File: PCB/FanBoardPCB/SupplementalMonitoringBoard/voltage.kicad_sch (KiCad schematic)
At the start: 6 parts, among them U1 OPA842xDBV

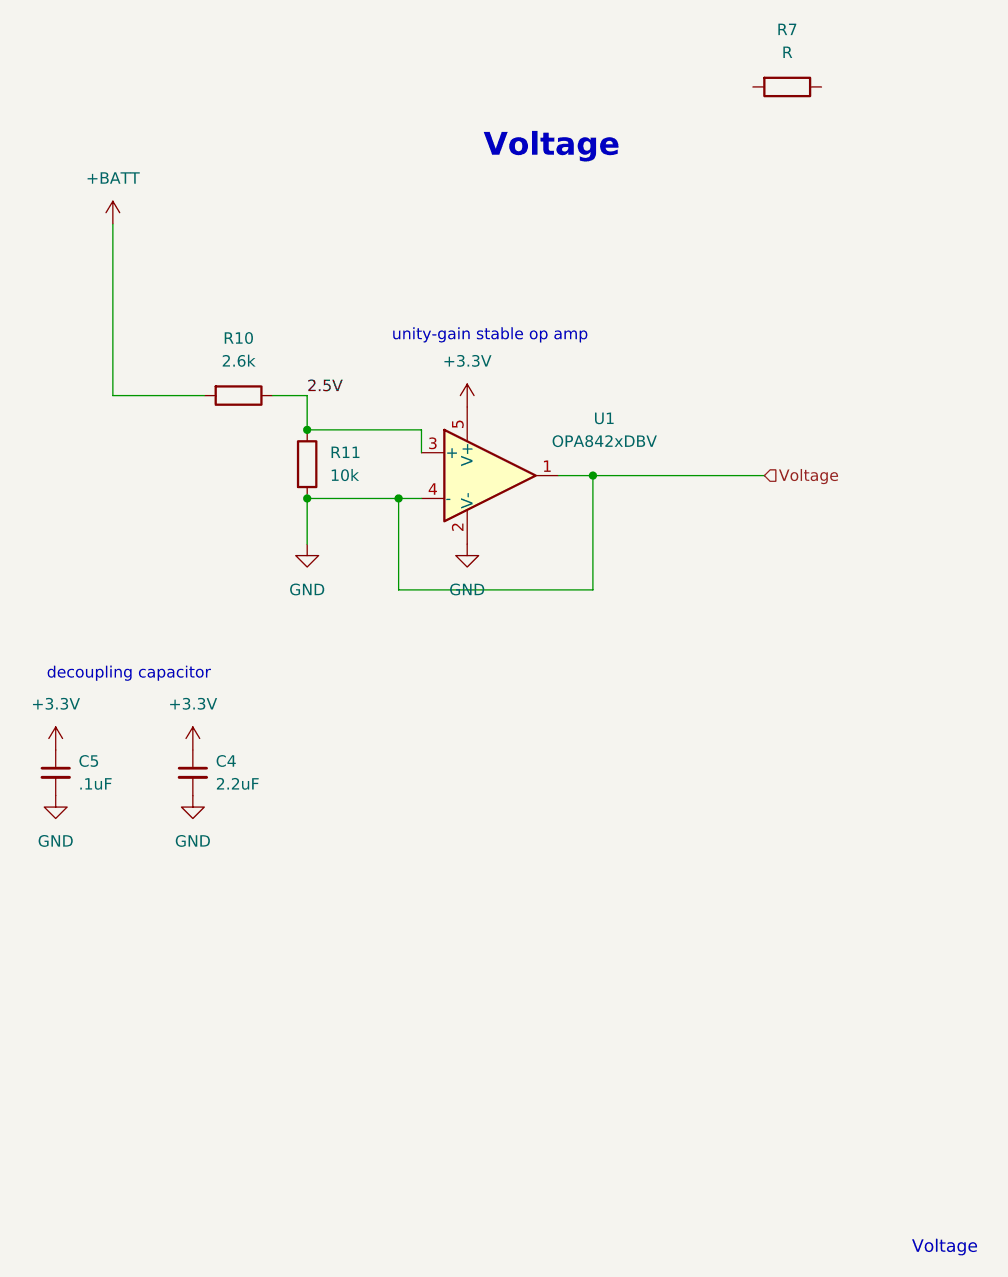
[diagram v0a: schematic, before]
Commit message: Supplemental Monitoring Board
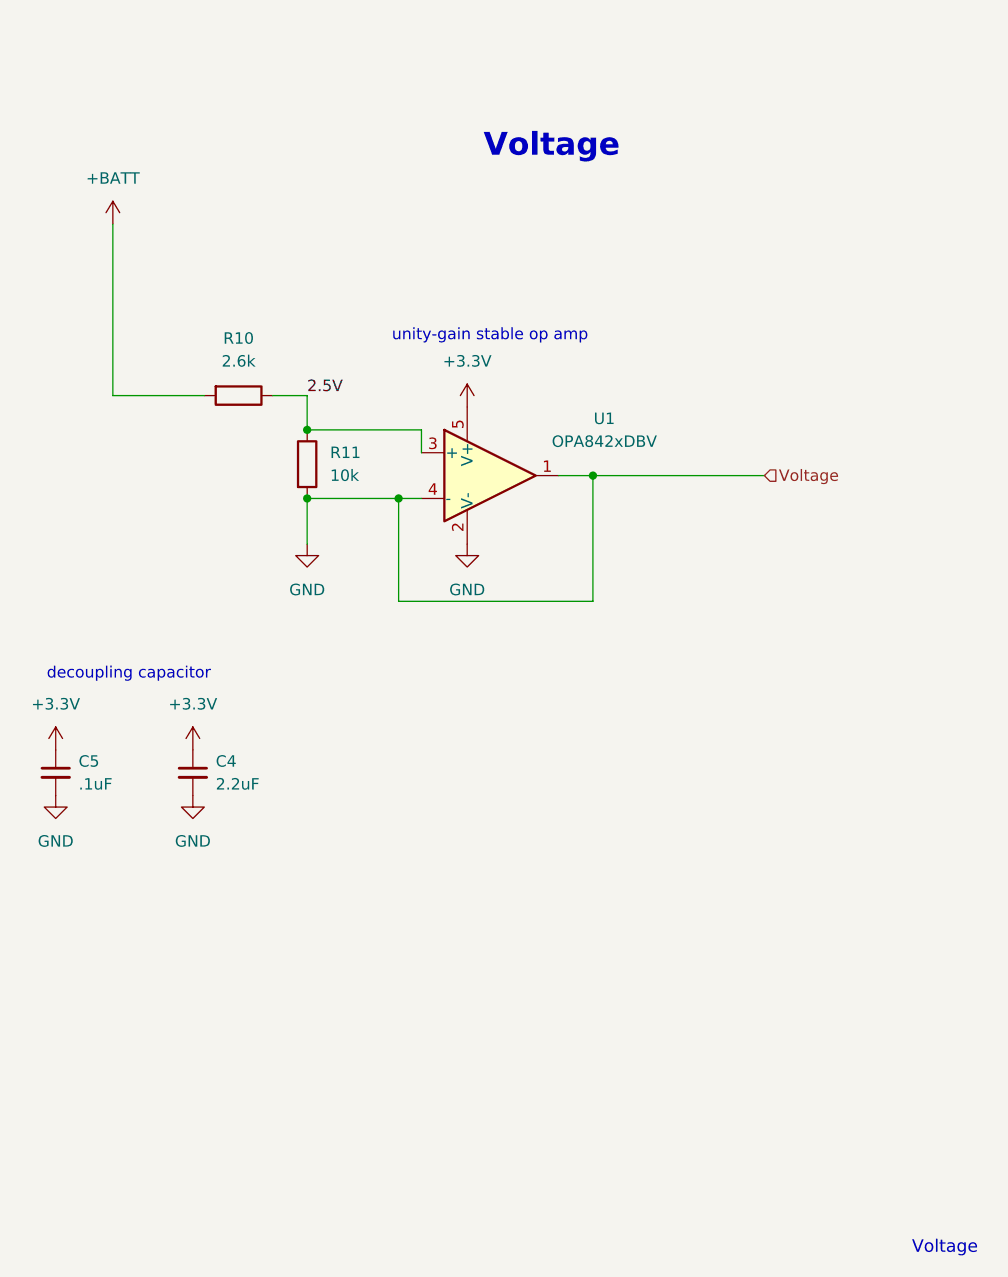
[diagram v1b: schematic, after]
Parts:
- removed R7: R, symbol Device:R
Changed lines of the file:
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@@
 	(wire
 		(pts
-			(xy 129.54 116.84) (xy 151.13 116.84)
-		)
-		(stroke
-			(width 0)
-			(type default)
-		)
-	)
-	(wire
-		(pts
-			(xy 129.54 106.68) (xy 129.54 116.84)
+			(xy 129.54 118.11) (xy 151.13 118.11)
+		)
+		(stroke
+			(width 0)
+			(type default)
+		)
+	)
+	(wire
+		(pts
+			(xy 129.54 106.68) (xy 129.54 118.11)
 		)
 		(stroke
@@
 	(wire
 		(pts
-			(xy 151.13 116.84) (xy 151.13 104.14)
+			(xy 151.13 118.11) (xy 151.13 104.14)
 		)
 		(stroke
@@
 					(unit 1)
 				)
-			)
-		)
-	)
-	(symbol
-		(lib_id "Device:R")
-		(at 172.72 60.96 270)
-		(unit 1)
-		(exclude_from_sim no)
-		(in_bom yes)
-		(on_board yes)
-		(dnp no)
-		(fields_autoplaced yes)
-		(property "Reference" "R7"
-			(at 172.72 54.61 90)
-			(effects
-				(font
-					(size 1.27 1.27)
-				)
-			)
-		)
-		(property "Value" "R"
-			(at 172.72 57.15 90)
-			(effects
-				(font
-					(size 1.27 1.27)
-				)
-			)
-		)
-		(property "Footprint" ""
-			(at 172.72 59.182 90)
-			(effects
-				(font
-					(size 1.27 1.27)
-				)
-				(hide yes)
-			)
-		)
-		(property "Datasheet" "~"
-			(at 172.72 60.96 0)
-			(effects
-				(font
-					(size 1.27 1.27)
-				)
-				(hide yes)
-			)
-		)
-		(property "Description" "Resistor"
-			(at 172.72 60.96 0)
-			(effects
-				(font
-					(size 1.27 1.27)
-				)
-				(hide yes)
-			)
-		)
-		(pin "1"
-		)
-		(pin "2"
-		)
-		(instances
-			(project "SupplementalMonitoringBoard"
-				(path "/aa0415d0-3287-4bc4-9a8e-766ada9ace2f/c3517b11-42d4-41ac-8608-60dda8052ca3"
-					(reference "R7")
-					(unit 1)
-				)
